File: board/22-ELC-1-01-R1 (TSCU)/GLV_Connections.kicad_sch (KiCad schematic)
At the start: 13 parts, among them Q1 AO3400A, Q2 AO3400A, Q3 AO3400A, Q4 AO3400A

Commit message: Ready for review
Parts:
- renumbered C6 to C11, Q1 to Q4, Q2 to Q5, Q3 to Q6, Q4 to Q7, R6 to R20, R7 to R21, R8 to R22, R9 to R23, R10 to R24, R11 to R25, R12 to R26, R13 to R27
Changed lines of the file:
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@@
   (symbol (lib_id "Device:R") (at 204.47 43.18 90) (unit 1)
     (in_bom yes) (on_board yes)
-    (property "Reference" "R7" (id 0) (at 204.47 45.72 90))
+    (property "Reference" "R21" (id 0) (at 204.47 45.72 90))
     (property "Value" "10k" (id 1) (at 204.47 43.18 90))
     (property "Footprint" "Resistor_SMD:R_0603_1608Metric_Pad0.98x0.95mm_HandSolder" (id 2) (at 204.47 44.958 90)
@@
   (symbol (lib_id "Device:Q_NMOS_GSD") (at 218.44 72.39 0) (unit 1)
     (in_bom yes) (on_board yes)
-    (property "Reference" "Q2" (id 0) (at 223.647 71.2216 0)
+    (property "Reference" "Q5" (id 0) (at 223.647 71.2216 0)
       (effects (font (size 1.27 1.27)) (justify left))
     )
@@
   (symbol (lib_id "Device:R") (at 205.74 72.39 270) (unit 1)
     (in_bom yes) (on_board yes)
-    (property "Reference" "R8" (id 0) (at 205.74 69.85 90))
+    (property "Reference" "R22" (id 0) (at 205.74 69.85 90))
     (property "Value" "10k" (id 1) (at 205.74 72.39 90))
     (property "Footprint" "Resistor_SMD:R_0603_1608Metric_Pad0.98x0.95mm_HandSolder" (id 2) (at 205.74 70.612 90)
@@
   (symbol (lib_id "power:GND") (at 215.9 83.82 0) (unit 1)
     (in_bom yes) (on_board yes)
-    (property "Reference" "#PWR028" (id 0) (at 215.9 90.17 0)
+    (property "Reference" "#PWR056" (id 0) (at 215.9 90.17 0)
       (effects (font (size 1.27 1.27)) hide)
     )
@@
   (symbol (lib_id "Device:R") (at 210.82 77.47 0) (unit 1)
     (in_bom yes) (on_board yes)
-    (property "Reference" "R11" (id 0) (at 212.598 76.3016 0)
+    (property "Reference" "R25" (id 0) (at 212.598 76.3016 0)
       (effects (font (size 1.27 1.27)) (justify left))
     )
@@
   (symbol (lib_id "power:GND") (at 215.9 54.61 0) (unit 1)
     (in_bom yes) (on_board yes)
-    (property "Reference" "#PWR027" (id 0) (at 215.9 60.96 0)
+    (property "Reference" "#PWR055" (id 0) (at 215.9 60.96 0)
       (effects (font (size 1.27 1.27)) hide)
     )
@@
   (symbol (lib_id "Device:R") (at 210.82 48.26 0) (unit 1)
     (in_bom yes) (on_board yes)
-    (property "Reference" "R10" (id 0) (at 212.598 47.0916 0)
+    (property "Reference" "R24" (id 0) (at 212.598 47.0916 0)
       (effects (font (size 1.27 1.27)) (justify left))
     )
@@
   (symbol (lib_id "Device:R") (at 196.85 132.08 270) (unit 1)
     (in_bom yes) (on_board yes)
-    (property "Reference" "R6" (id 0) (at 196.85 129.54 90))
+    (property "Reference" "R20" (id 0) (at 196.85 129.54 90))
     (property "Value" "1k" (id 1) (at 196.85 132.08 90))
     (property "Footprint" "Resistor_SMD:R_0603_1608Metric_Pad0.98x0.95mm_HandSolder" (id 2) (at 196.85 130.302 90)
@@
   (symbol (lib_id "Device:C_Small") (at 203.2 135.89 0) (unit 1)
     (in_bom yes) (on_board yes)
-    (property "Reference" "C6" (id 0) (at 197.3834 135.89 90))
+    (property "Reference" "C11" (id 0) (at 197.3834 135.89 90))
     (property "Value" "0.1uf" (id 1) (at 199.6948 135.89 90))
     (property "Footprint" "Capacitor_SMD:C_0603_1608Metric_Pad1.08x0.95mm_HandSolder" (id 2) (at 203.2 135.89 0)
@@
   (symbol (lib_id "Device:R") (at 210.82 135.89 0) (unit 1)
     (in_bom yes) (on_board yes)
-    (property "Reference" "R13" (id 0) (at 208.28 135.89 90))
+    (property "Reference" "R27" (id 0) (at 208.28 135.89 90))
     (property "Value" "100k" (id 1) (at 210.82 135.89 90))
     (property "Footprint" "Resistor_SMD:R_0603_1608Metric_Pad0.98x0.95mm_HandSolder" (id 2) (at 209.042 135.89 90)
@@
   (symbol (lib_id "power:GND") (at 207.01 139.7 0) (unit 1)
     (in_bom yes) (on_board yes)
-    (property "Reference" "#PWR026" (id 0) (at 207.01 146.05 0)
+    (property "Reference" "#PWR054" (id 0) (at 207.01 146.05 0)
       (effects (font (size 1.27 1.27)) hide)
     )
@@
   (symbol (lib_id "power:GND") (at 220.98 137.16 0) (unit 1)
     (in_bom yes) (on_board yes)
-    (property "Reference" "#PWR030" (id 0) (at 220.98 143.51 0)
+    (property "Reference" "#PWR058" (id 0) (at 220.98 143.51 0)
       (effects (font (size 1.27 1.27)) hide)
     )
@@
   (symbol (lib_id "Device:Q_NMOS_GSD") (at 218.44 43.18 0) (unit 1)
     (in_bom yes) (on_board yes)
-    (property "Reference" "Q1" (id 0) (at 223.647 42.0116 0)
+    (property "Reference" "Q4" (id 0) (at 223.647 42.0116 0)
       (effects (font (size 1.27 1.27)) (justify left))
     )
@@
   (symbol (lib_id "Device:Q_NMOS_GSD") (at 218.44 132.08 0) (unit 1)
     (in_bom yes) (on_board yes)
-    (property "Reference" "Q4" (id 0) (at 223.647 130.9116 0)
+    (property "Reference" "Q7" (id 0) (at 223.647 130.9116 0)
       (effects (font (size 1.27 1.27)) (justify left))
     )
@@
   (symbol (lib_id "Device:Q_NMOS_GSD") (at 218.44 101.6 0) (unit 1)
     (in_bom yes) (on_board yes)
-    (property "Reference" "Q3" (id 0) (at 223.647 100.4316 0)
+    (property "Reference" "Q6" (id 0) (at 223.647 100.4316 0)
       (effects (font (size 1.27 1.27)) (justify left))
     )
@@
   (symbol (lib_id "Device:R") (at 205.74 101.6 270) (unit 1)
     (in_bom yes) (on_board yes)
-    (property "Reference" "R9" (id 0) (at 205.74 99.06 90))
+    (property "Reference" "R23" (id 0) (at 205.74 99.06 90))
     (property "Value" "10k" (id 1) (at 205.74 101.6 90))
     (property "Footprint" "Resistor_SMD:R_0603_1608Metric_Pad0.98x0.95mm_HandSolder" (id 2) (at 205.74 99.822 90)
@@
   (symbol (lib_id "power:GND") (at 215.9 113.03 0) (unit 1)
     (in_bom yes) (on_board yes)
-    (property "Reference" "#PWR029" (id 0) (at 215.9 119.38 0)
+    (property "Reference" "#PWR057" (id 0) (at 215.9 119.38 0)
       (effects (font (size 1.27 1.27)) hide)
     )
@@
   (symbol (lib_id "Device:R") (at 210.82 106.68 0) (unit 1)
     (in_bom yes) (on_board yes)
-    (property "Reference" "R12" (id 0) (at 212.598 105.5116 0)
-      (effects (font (size 1.27 1.27)) (justify left))
-    )
+    (property "Reference" "R26" (id 0) (at 212.598 105.5116 0)
+      (effects (font (size 1.27 1.27)) (justify left))
+    )

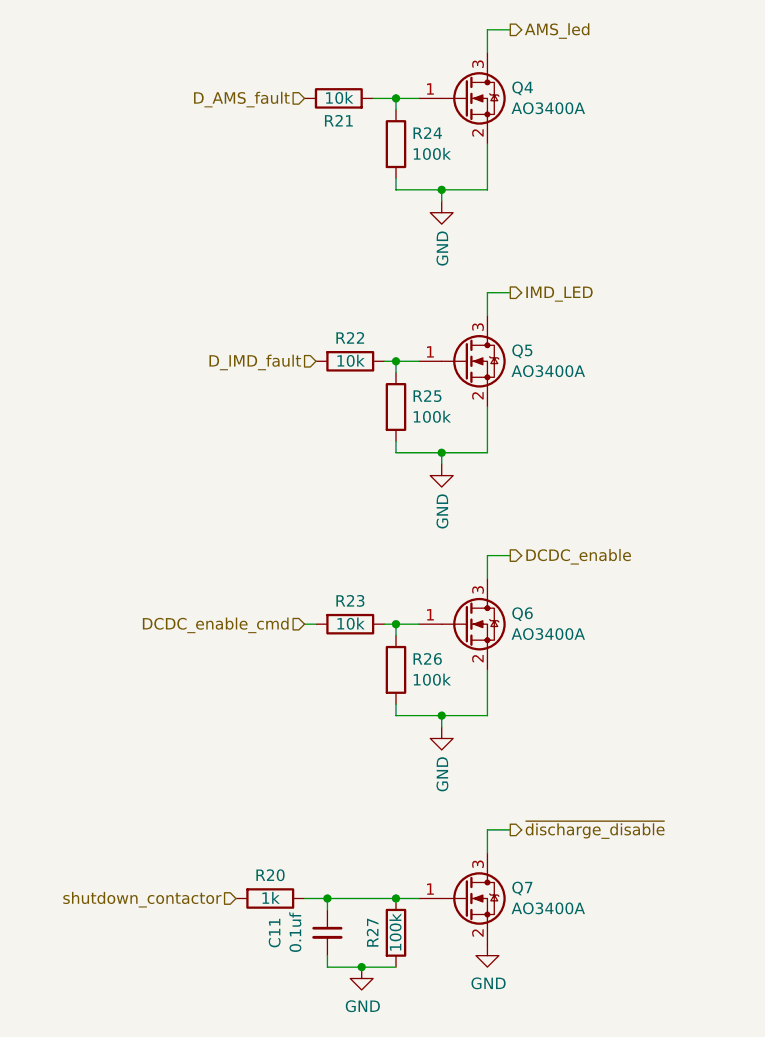
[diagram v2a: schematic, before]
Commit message: All good except need to switch everything to accepting 24v power
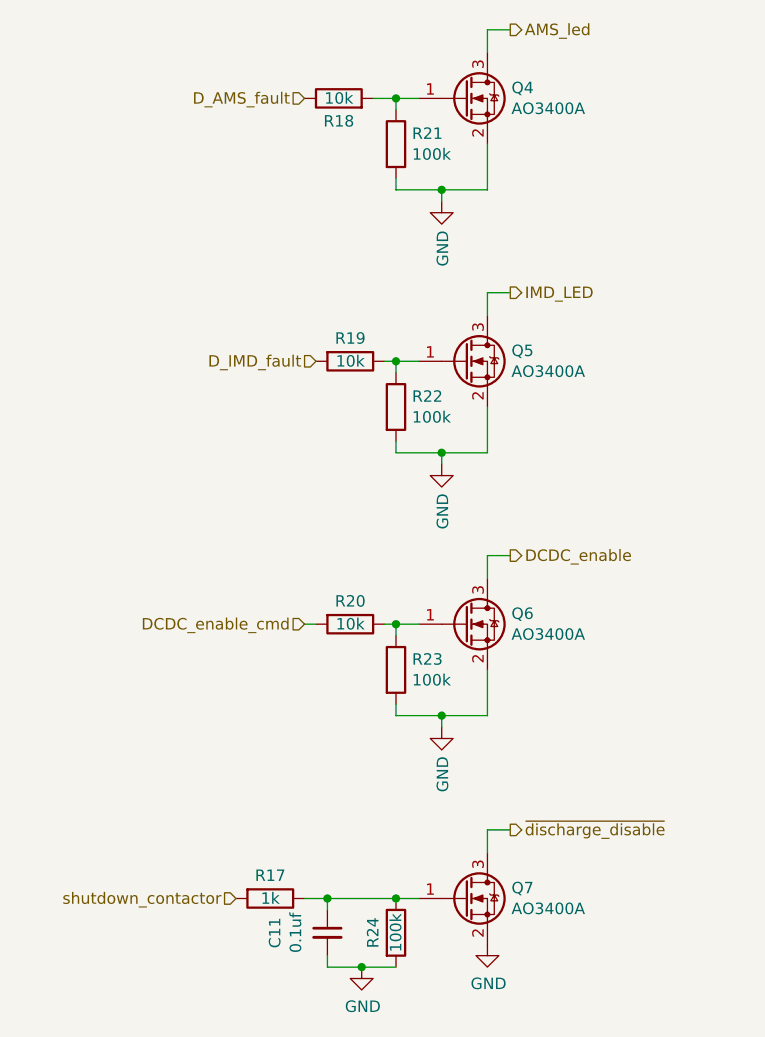
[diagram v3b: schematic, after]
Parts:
- renumbered R20 to R17, R21 to R18, R22 to R19, R23 to R20, R24 to R21, R25 to R22, R26 to R23, R27 to R24
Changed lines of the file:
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@@
   (symbol (lib_id "Device:R") (at 204.47 43.18 90) (unit 1)
     (in_bom yes) (on_board yes)
-    (property "Reference" "R21" (id 0) (at 204.47 45.72 90))
+    (property "Reference" "R18" (id 0) (at 204.47 45.72 90))
     (property "Value" "10k" (id 1) (at 204.47 43.18 90))
     (property "Footprint" "Resistor_SMD:R_0603_1608Metric_Pad0.98x0.95mm_HandSolder" (id 2) (at 204.47 44.958 90)
@@
   (symbol (lib_id "Device:R") (at 205.74 72.39 270) (unit 1)
     (in_bom yes) (on_board yes)
-    (property "Reference" "R22" (id 0) (at 205.74 69.85 90))
+    (property "Reference" "R19" (id 0) (at 205.74 69.85 90))
     (property "Value" "10k" (id 1) (at 205.74 72.39 90))
     (property "Footprint" "Resistor_SMD:R_0603_1608Metric_Pad0.98x0.95mm_HandSolder" (id 2) (at 205.74 70.612 90)
@@
   (symbol (lib_id "Device:R") (at 210.82 77.47 0) (unit 1)
     (in_bom yes) (on_board yes)
-    (property "Reference" "R25" (id 0) (at 212.598 76.3016 0)
+    (property "Reference" "R22" (id 0) (at 212.598 76.3016 0)
       (effects (font (size 1.27 1.27)) (justify left))
     )
@@
   (symbol (lib_id "Device:R") (at 210.82 48.26 0) (unit 1)
     (in_bom yes) (on_board yes)
-    (property "Reference" "R24" (id 0) (at 212.598 47.0916 0)
+    (property "Reference" "R21" (id 0) (at 212.598 47.0916 0)
       (effects (font (size 1.27 1.27)) (justify left))
     )
@@
   (symbol (lib_id "Device:R") (at 196.85 132.08 270) (unit 1)
     (in_bom yes) (on_board yes)
-    (property "Reference" "R20" (id 0) (at 196.85 129.54 90))
+    (property "Reference" "R17" (id 0) (at 196.85 129.54 90))
     (property "Value" "1k" (id 1) (at 196.85 132.08 90))
     (property "Footprint" "Resistor_SMD:R_0603_1608Metric_Pad0.98x0.95mm_HandSolder" (id 2) (at 196.85 130.302 90)
@@
   (symbol (lib_id "Device:R") (at 210.82 135.89 0) (unit 1)
     (in_bom yes) (on_board yes)
-    (property "Reference" "R27" (id 0) (at 208.28 135.89 90))
+    (property "Reference" "R24" (id 0) (at 208.28 135.89 90))
     (property "Value" "100k" (id 1) (at 210.82 135.89 90))
     (property "Footprint" "Resistor_SMD:R_0603_1608Metric_Pad0.98x0.95mm_HandSolder" (id 2) (at 209.042 135.89 90)
@@
   (symbol (lib_id "Device:R") (at 205.74 101.6 270) (unit 1)
     (in_bom yes) (on_board yes)
-    (property "Reference" "R23" (id 0) (at 205.74 99.06 90))
+    (property "Reference" "R20" (id 0) (at 205.74 99.06 90))
     (property "Value" "10k" (id 1) (at 205.74 101.6 90))
     (property "Footprint" "Resistor_SMD:R_0603_1608Metric_Pad0.98x0.95mm_HandSolder" (id 2) (at 205.74 99.822 90)
@@
   (symbol (lib_id "Device:R") (at 210.82 106.68 0) (unit 1)
     (in_bom yes) (on_board yes)
-    (property "Reference" "R26" (id 0) (at 212.598 105.5116 0)
-      (effects (font (size 1.27 1.27)) (justify left))
-    )
+    (property "Reference" "R23" (id 0) (at 212.598 105.5116 0)
+      (effects (font (size 1.27 1.27)) (justify left))
+    )

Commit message: Finalized schematic, started board layout
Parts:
- C11: footprint Capacitor_SMD:C_0603_1608Metric_Pad1.08x0.95mm_HandSolder -> Capacitor_SMD:C_0402_1005Metric
- R17, R18, R19, R20, R21, R22, R23, R24: footprint Resistor_SMD:R_0603_1608Metric_Pad0.98x0.95mm_HandSolder -> FixedTextSizes:R_0402_1005Metric
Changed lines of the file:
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@@
     (property "Reference" "R18" (id 0) (at 204.47 45.72 90))
     (property "Value" "10k" (id 1) (at 204.47 43.18 90))
-    (property "Footprint" "Resistor_SMD:R_0603_1608Metric_Pad0.98x0.95mm_HandSolder" (id 2) (at 204.47 44.958 90)
+    (property "Footprint" "FixedTextSizes:R_0402_1005Metric" (id 2) (at 204.47 44.958 90)
       (effects (font (size 1.27 1.27)) hide)
     )
@@
     (property "Reference" "R19" (id 0) (at 205.74 69.85 90))
     (property "Value" "10k" (id 1) (at 205.74 72.39 90))
-    (property "Footprint" "Resistor_SMD:R_0603_1608Metric_Pad0.98x0.95mm_HandSolder" (id 2) (at 205.74 70.612 90)
+    (property "Footprint" "FixedTextSizes:R_0402_1005Metric" (id 2) (at 205.74 70.612 90)
       (effects (font (size 1.27 1.27)) hide)
     )
@@
   (symbol (lib_id "power:GND") (at 215.9 83.82 0) (unit 1)
     (in_bom yes) (on_board yes)
-    (property "Reference" "#PWR056" (id 0) (at 215.9 90.17 0)
+    (property "Reference" "#PWR055" (id 0) (at 215.9 90.17 0)
       (effects (font (size 1.27 1.27)) hide)
     )
@@
       (effects (font (size 1.27 1.27)) (justify left))
     )
-    (property "Footprint" "Resistor_SMD:R_0603_1608Metric_Pad0.98x0.95mm_HandSolder" (id 2) (at 209.042 77.47 90)
+    (property "Footprint" "FixedTextSizes:R_0402_1005Metric" (id 2) (at 209.042 77.47 90)
       (effects (font (size 1.27 1.27)) hide)
     )
@@
   (symbol (lib_id "power:GND") (at 215.9 54.61 0) (unit 1)
     (in_bom yes) (on_board yes)
-    (property "Reference" "#PWR055" (id 0) (at 215.9 60.96 0)
+    (property "Reference" "#PWR054" (id 0) (at 215.9 60.96 0)
       (effects (font (size 1.27 1.27)) hide)
     )
@@
       (effects (font (size 1.27 1.27)) (justify left))
     )
-    (property "Footprint" "Resistor_SMD:R_0603_1608Metric_Pad0.98x0.95mm_HandSolder" (id 2) (at 209.042 48.26 90)
+    (property "Footprint" "FixedTextSizes:R_0402_1005Metric" (id 2) (at 209.042 48.26 90)
       (effects (font (size 1.27 1.27)) hide)
     )
@@
     (property "Reference" "R17" (id 0) (at 196.85 129.54 90))
     (property "Value" "1k" (id 1) (at 196.85 132.08 90))
-    (property "Footprint" "Resistor_SMD:R_0603_1608Metric_Pad0.98x0.95mm_HandSolder" (id 2) (at 196.85 130.302 90)
+    (property "Footprint" "FixedTextSizes:R_0402_1005Metric" (id 2) (at 196.85 130.302 90)
       (effects (font (size 1.27 1.27)) hide)
     )
@@
     (property "Reference" "C11" (id 0) (at 197.3834 135.89 90))
     (property "Value" "0.1uf" (id 1) (at 199.6948 135.89 90))
-    (property "Footprint" "Capacitor_SMD:C_0603_1608Metric_Pad1.08x0.95mm_HandSolder" (id 2) (at 203.2 135.89 0)
+    (property "Footprint" "Capacitor_SMD:C_0402_1005Metric" (id 2) (at 203.2 135.89 0)
       (effects (font (size 1.27 1.27)) hide)
     )
@@
     (property "Reference" "R24" (id 0) (at 208.28 135.89 90))
     (property "Value" "100k" (id 1) (at 210.82 135.89 90))
-    (property "Footprint" "Resistor_SMD:R_0603_1608Metric_Pad0.98x0.95mm_HandSolder" (id 2) (at 209.042 135.89 90)
+    (property "Footprint" "FixedTextSizes:R_0402_1005Metric" (id 2) (at 209.042 135.89 90)
       (effects (font (size 1.27 1.27)) hide)
     )
@@
   (symbol (lib_id "power:GND") (at 207.01 139.7 0) (unit 1)
     (in_bom yes) (on_board yes)
-    (property "Reference" "#PWR054" (id 0) (at 207.01 146.05 0)
+    (property "Reference" "#PWR053" (id 0) (at 207.01 146.05 0)
       (effects (font (size 1.27 1.27)) hide)
     )
@@
   (symbol (lib_id "power:GND") (at 220.98 137.16 0) (unit 1)
     (in_bom yes) (on_board yes)
-    (property "Reference" "#PWR058" (id 0) (at 220.98 143.51 0)
+    (property "Reference" "#PWR057" (id 0) (at 220.98 143.51 0)
       (effects (font (size 1.27 1.27)) hide)
     )
@@
     (property "Reference" "R20" (id 0) (at 205.74 99.06 90))
     (property "Value" "10k" (id 1) (at 205.74 101.6 90))
-    (property "Footprint" "Resistor_SMD:R_0603_1608Metric_Pad0.98x0.95mm_HandSolder" (id 2) (at 205.74 99.822 90)
+    (property "Footprint" "FixedTextSizes:R_0402_1005Metric" (id 2) (at 205.74 99.822 90)
       (effects (font (size 1.27 1.27)) hide)
     )
@@
   (symbol (lib_id "power:GND") (at 215.9 113.03 0) (unit 1)
     (in_bom yes) (on_board yes)
-    (property "Reference" "#PWR057" (id 0) (at 215.9 119.38 0)
+    (property "Reference" "#PWR056" (id 0) (at 215.9 119.38 0)
       (effects (font (size 1.27 1.27)) hide)
     )
@@
       (effects (font (size 1.27 1.27)) (justify left))
     )
-    (property "Footprint" "Resistor_SMD:R_0603_1608Metric_Pad0.98x0.95mm_HandSolder" (id 2) (at 209.042 106.68 90)
-      (effects (font (size 1.27 1.27)) hide)
-    )
+    (property "Footprint" "FixedTextSizes:R_0402_1005Metric" (id 2) (at 209.042 106.68 90)
+      (effects (font (size 1.27 1.27)) hide)
+    )

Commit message: More progress
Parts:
- C11: footprint Capacitor_SMD:C_0402_1005Metric -> FixedTextSizes:C_0402_1005Metric_Pad0.74x0.62mm_HandSolder_Reasonable_Text_Size
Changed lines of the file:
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@@
   (symbol (lib_id "power:GND") (at 215.9 83.82 0) (unit 1)
     (in_bom yes) (on_board yes)
-    (property "Reference" "#PWR055" (id 0) (at 215.9 90.17 0)
+    (property "Reference" "#PWR058" (id 0) (at 215.9 90.17 0)
       (effects (font (size 1.27 1.27)) hide)
     )
@@
   (symbol (lib_id "power:GND") (at 215.9 54.61 0) (unit 1)
     (in_bom yes) (on_board yes)
-    (property "Reference" "#PWR054" (id 0) (at 215.9 60.96 0)
+    (property "Reference" "#PWR057" (id 0) (at 215.9 60.96 0)
       (effects (font (size 1.27 1.27)) hide)
     )
@@
     (property "Reference" "C11" (id 0) (at 197.3834 135.89 90))
     (property "Value" "0.1uf" (id 1) (at 199.6948 135.89 90))
-    (property "Footprint" "Capacitor_SMD:C_0402_1005Metric" (id 2) (at 203.2 135.89 0)
+    (property "Footprint" "FixedTextSizes:C_0402_1005Metric_Pad0.74x0.62mm_HandSolder_Reasonable_Text_Size" (id 2) (at 203.2 135.89 0)
       (effects (font (size 1.27 1.27)) hide)
     )
@@
   (symbol (lib_id "power:GND") (at 207.01 139.7 0) (unit 1)
     (in_bom yes) (on_board yes)
-    (property "Reference" "#PWR053" (id 0) (at 207.01 146.05 0)
+    (property "Reference" "#PWR056" (id 0) (at 207.01 146.05 0)
       (effects (font (size 1.27 1.27)) hide)
     )
@@
   (symbol (lib_id "power:GND") (at 220.98 137.16 0) (unit 1)
     (in_bom yes) (on_board yes)
-    (property "Reference" "#PWR057" (id 0) (at 220.98 143.51 0)
+    (property "Reference" "#PWR060" (id 0) (at 220.98 143.51 0)
       (effects (font (size 1.27 1.27)) hide)
     )
@@
   (symbol (lib_id "power:GND") (at 215.9 113.03 0) (unit 1)
     (in_bom yes) (on_board yes)
-    (property "Reference" "#PWR056" (id 0) (at 215.9 119.38 0)
-      (effects (font (size 1.27 1.27)) hide)
-    )
+    (property "Reference" "#PWR059" (id 0) (at 215.9 119.38 0)
+      (effects (font (size 1.27 1.27)) hide)
+    )
